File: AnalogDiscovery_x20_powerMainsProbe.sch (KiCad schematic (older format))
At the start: 22 parts, among them J1 Conn_02x15_Counter_Clockwise, J2 Conn_01x03_Female, J3 Conn_01x03_Female, J4 Conn_01x03_Male, J5 Conn_01x03_Male, J6 Conn_02x03_Counter_Clockwise

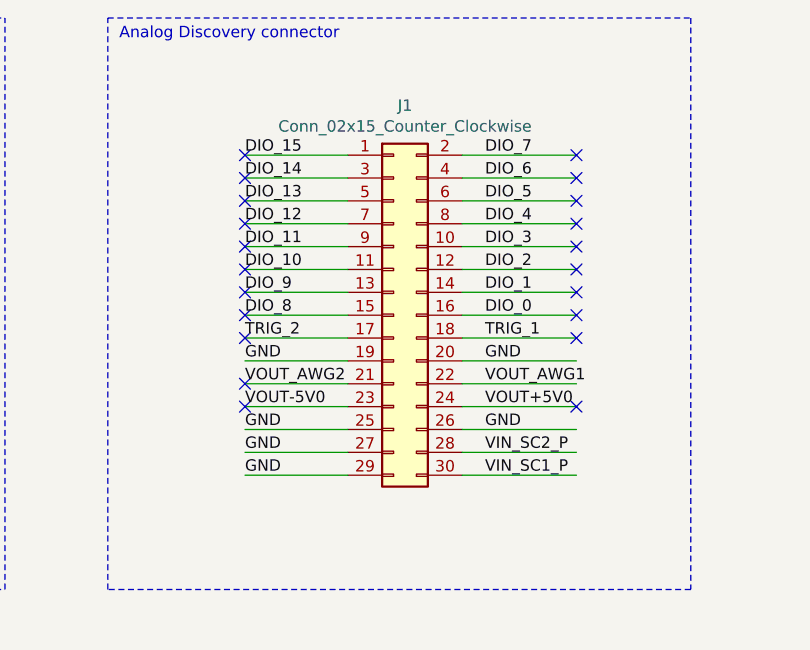
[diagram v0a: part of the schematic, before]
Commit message: Solved issue #10
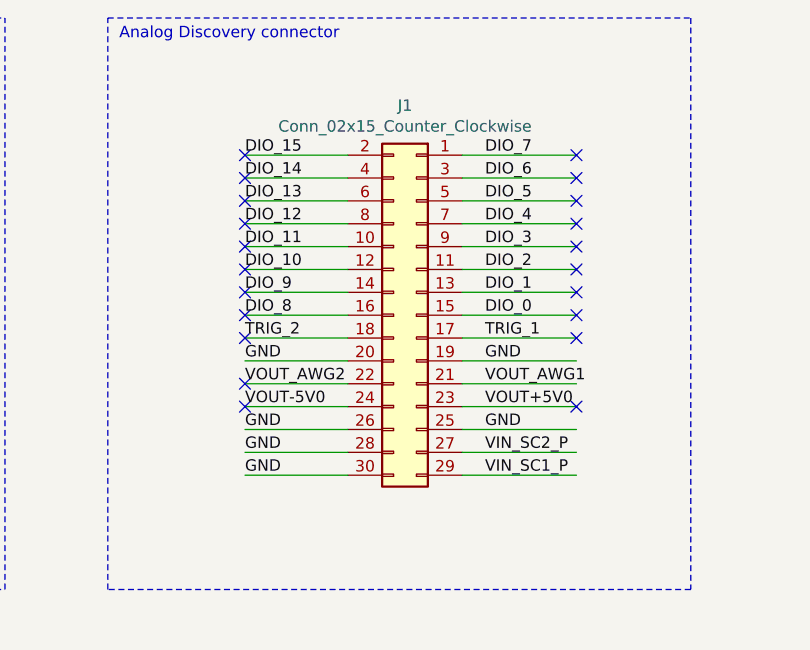
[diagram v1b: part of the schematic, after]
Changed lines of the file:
@@
 L Connector_Generic:Conn_02x15_Odd_Even J1
 U 1 1 5D94C9D0
-P 8750 2050
-F 0 "J1" H 8800 2967 50  0000 C CNN
-F 1 "Conn_02x15_Counter_Clockwise" H 8800 2876 50  0000 C CNN
-F 2 "Connector_PinSocket_2.54mm:PinSocket_2x15_P2.54mm_Horizontal" H 8750 2050 50  0001 C CNN
-F 3 "RS:765-5783" H 8750 2050 50  0001 C CNN
-	1    8750 2050
-	1    0    0    -1
+P 8850 2050
+F 0 "J1" H 8900 2967 50  0000 C CNN
+F 1 "Conn_02x15_Counter_Clockwise" H 8900 2876 50  0000 C CNN
+F 2 "Connector_PinSocket_2.54mm:PinSocket_2x15_P2.54mm_Horizontal" H 8850 2050 50  0001 C CNN
+F 3 "RS:765-5783" H 8850 2050 50  0001 C CNN
+	1    8850 2050
+	-1   0    0    -1
 $EndComp
 Wire Wire Line
@@
 Text Label 8100 2050 0    50   ~ 0
 DIO_8
-Wire Wire Line
-	8100 2750 8550 2750
-Wire Wire Line
-	8100 2650 8550 2650
-Wire Wire Line
-	8100 2550 8550 2550
-Wire Wire Line
-	8100 2450 8550 2450
-Wire Wire Line
-	8100 2350 8550 2350
-Wire Wire Line
-	8100 2250 8550 2250
-Wire Wire Line
-	8100 2150 8550 2150
-Wire Wire Line
-	8100 2050 8550 2050
-Wire Wire Line
-	8100 1950 8550 1950
-Wire Wire Line
-	8100 1850 8550 1850
-Wire Wire Line
-	8100 1750 8550 1750
-Wire Wire Line
-	8100 1650 8550 1650
-Wire Wire Line
-	8100 1550 8550 1550
-Wire Wire Line
-	8100 1450 8550 1450
-Wire Wire Line
-	8100 1350 8550 1350
 Text Label 9150 2250 0    50   ~ 0
 GND
@@
 Text Notes 8050 4100 0    50   ~ 0
 Tunning connector
+Wire Wire Line
+	8100 1350 8550 1350
+Wire Wire Line
+	8100 1450 8550 1450
+Wire Wire Line
+	8100 1550 8550 1550
+Wire Wire Line
+	8100 1650 8550 1650
+Wire Wire Line
+	8100 1750 8550 1750
+Wire Wire Line
+	8100 1850 8550 1850
+Wire Wire Line
+	8100 1950 8550 1950
+Wire Wire Line
+	8100 2050 8550 2050
+Wire Wire Line
+	8100 2150 8550 2150
+Wire Wire Line
+	8100 2250 8550 2250
+Wire Wire Line
+	8100 2350 8550 2350
+Wire Wire Line
+	8100 2450 8550 2450
+Wire Wire Line
+	8100 2550 8550 2550
+Wire Wire Line
+	8100 2650 8550 2650
+Wire Wire Line
+	8100 2750 8550 2750
 $EndSCHEMATC

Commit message: Issue #9 fixed. The resistor pin separation has been change from 6 to 10mm
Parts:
- R1, R2, R3, R4, R5, R6: footprint Resistor_THT:R_Axial_DIN0207_L6.3mm_D2.5mm_P7.62mm_Horizontal -> Resistor_THT:R_Axial_DIN0207_L6.3mm_D2.5mm_P10.16mm_Horizontal
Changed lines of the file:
@@
 F 0 "R1" V 2393 1950 50  0000 C CNN
 F 1 "9M1" V 2484 1950 50  0000 C CNN
-F 2 "Resistor_THT:R_Axial_DIN0207_L6.3mm_D2.5mm_P7.62mm_Horizontal" V 2530 1950 50  0001 C CNN
+F 2 "Resistor_THT:R_Axial_DIN0207_L6.3mm_D2.5mm_P10.16mm_Horizontal" V 2530 1950 50  0001 C CNN
 F 3 "~" H 2600 1950 50  0001 C CNN
 	1    2600 1950
@@
 F 0 "R2" V 2943 1950 50  0000 C CNN
 F 1 "220k" V 3034 1950 50  0000 C CNN
-F 2 "Resistor_THT:R_Axial_DIN0207_L6.3mm_D2.5mm_P7.62mm_Horizontal" V 3080 1950 50  0001 C CNN
+F 2 "Resistor_THT:R_Axial_DIN0207_L6.3mm_D2.5mm_P10.16mm_Horizontal" V 3080 1950 50  0001 C CNN
 F 3 "~" H 3150 1950 50  0001 C CNN
 	1    3150 1950
@@
 F 0 "R3" H 4780 2304 50  0000 R CNN
 F 1 "1M" H 4780 2395 50  0000 R CNN
-F 2 "Resistor_THT:R_Axial_DIN0207_L6.3mm_D2.5mm_P7.62mm_Horizontal" V 4780 2350 50  0001 C CNN
+F 2 "Resistor_THT:R_Axial_DIN0207_L6.3mm_D2.5mm_P10.16mm_Horizontal" V 4780 2350 50  0001 C CNN
 F 3 "~" H 4850 2350 50  0001 C CNN
 	1    4850 2350
@@
 F 0 "R4" V 2843 4800 50  0000 C CNN
 F 1 "9M1" V 2934 4800 50  0000 C CNN
-F 2 "Resistor_THT:R_Axial_DIN0207_L6.3mm_D2.5mm_P7.62mm_Horizontal" V 2980 4800 50  0001 C CNN
+F 2 "Resistor_THT:R_Axial_DIN0207_L6.3mm_D2.5mm_P10.16mm_Horizontal" V 2980 4800 50  0001 C CNN
 F 3 "~" H 3050 4800 50  0001 C CNN
 	1    3050 4800
@@
 F 0 "R5" V 3393 4800 50  0000 C CNN
 F 1 "220k" V 3484 4800 50  0000 C CNN
-F 2 "Resistor_THT:R_Axial_DIN0207_L6.3mm_D2.5mm_P7.62mm_Horizontal" V 3530 4800 50  0001 C CNN
+F 2 "Resistor_THT:R_Axial_DIN0207_L6.3mm_D2.5mm_P10.16mm_Horizontal" V 3530 4800 50  0001 C CNN
 F 3 "~" H 3600 4800 50  0001 C CNN
 	1    3600 4800
@@
 F 0 "R6" H 5230 5154 50  0000 R CNN
 F 1 "1M" H 5230 5245 50  0000 R CNN
-F 2 "Resistor_THT:R_Axial_DIN0207_L6.3mm_D2.5mm_P7.62mm_Horizontal" V 5230 5200 50  0001 C CNN
+F 2 "Resistor_THT:R_Axial_DIN0207_L6.3mm_D2.5mm_P10.16mm_Horizontal" V 5230 5200 50  0001 C CNN
 F 3 "~" H 5300 5200 50  0001 C CNN
 	1    5300 5200

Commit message: Footprint fixed for potentiometers
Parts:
- RV2, RV3: footprint Potentiometer_THT:Potentiometer_Runtron_RM-065_Vertical -> my_footprint_library:Potentiometer_Bourns_3306P-1-504
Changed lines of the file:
@@
 F 0 "RV2" V 3585 1950 50  0000 C CNN
 F 1 "500k" V 3494 1950 50  0000 C CNN
-F 2 "Potentiometer_THT:Potentiometer_Runtron_RM-065_Vertical" H 3700 1950 50  0001 C CNN
+F 2 "my_footprint_library:Potentiometer_Bourns_3306P-1-504" H 3700 1950 50  0001 C CNN
 F 3 "RS:488-5388" H 3700 1950 50  0001 C CNN
 	1    3700 1950
@@
 F 0 "RV3" V 4035 4800 50  0000 C CNN
 F 1 "500k" V 3944 4800 50  0000 C CNN
-F 2 "Potentiometer_THT:Potentiometer_Runtron_RM-065_Vertical" H 4150 4800 50  0001 C CNN
+F 2 "my_footprint_library:Potentiometer_Bourns_3306P-1-504" H 4150 4800 50  0001 C CNN
 F 3 "RS:488-5388" H 4150 4800 50  0001 C CNN
 	1    4150 4800
